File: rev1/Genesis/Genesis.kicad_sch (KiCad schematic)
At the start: 0 parts

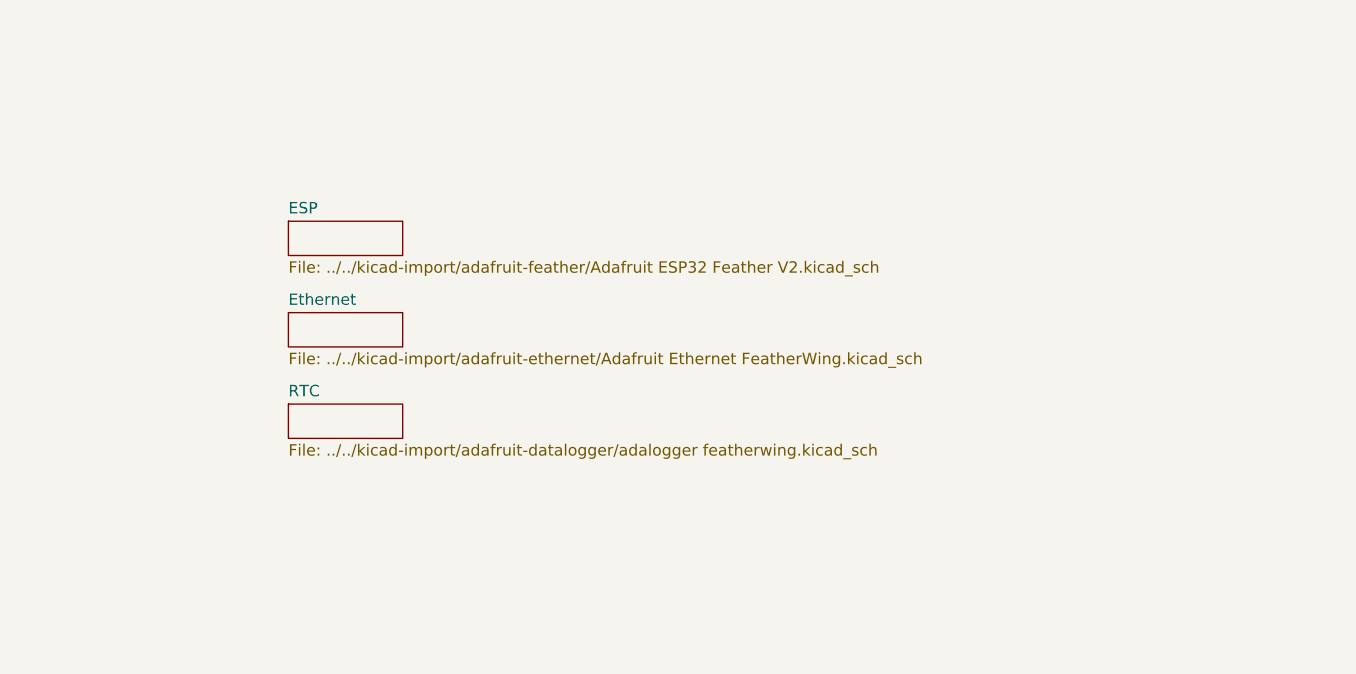
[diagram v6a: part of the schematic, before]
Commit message: Start adding heirarchical labels. Add notes to check sub-feather jumpers.
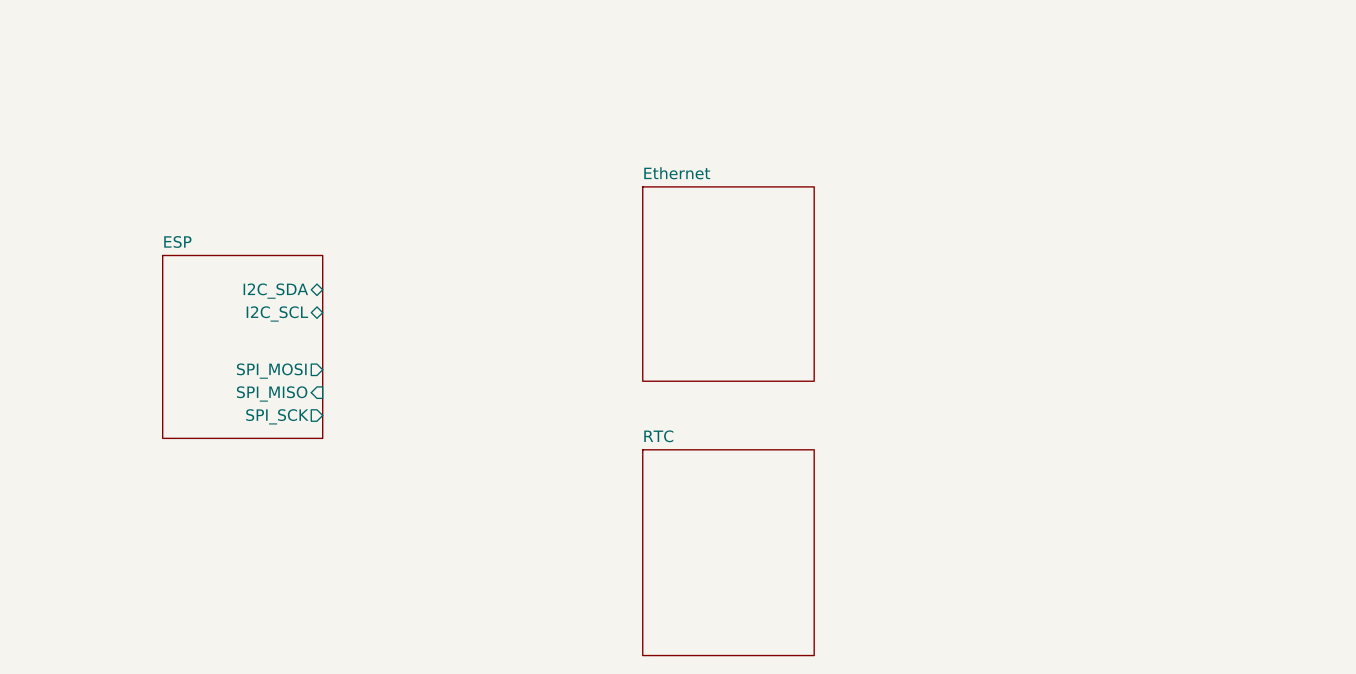
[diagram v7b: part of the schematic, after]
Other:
- sheet ESP ports: added I2C_SCL, I2C_SDA, SPI_MISO, SPI_MOSI, SPI_SCK; removed none
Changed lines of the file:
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@@
 	)
 	(sheet
-		(at 66.04 62.23)
-		(size 12.7 3.81)
+		(at 52.07 66.04)
+		(size 17.78 20.32)
 		(exclude_from_sim no)
 		(in_bom yes)
@@
 		)
 		(property "Sheetname" "ESP"
-			(at 66.04 61.5184 0)
+			(at 52.07 65.3284 0)
 			(effects
 				(font
@@
 		)
 		(property "Sheetfile" "../../kicad-import/adafruit-feather/Adafruit ESP32 Feather V2.kicad_sch"
-			(at 66.04 66.6246 0)
+			(at 52.07 86.9446 0)
 			(effects
 				(font
@@
 				)
 				(justify left top)
+				(hide yes)
+			)
+		)
+		(pin "I2C_SDA" bidirectional
+			(at 69.85 69.85 0)
+			(effects
+				(font
+					(size 1.27 1.27)
+				)
+				(justify right)
+			)
+		)
+		(pin "SPI_MOSI" output
+			(at 69.85 78.74 0)
+			(effects
+				(font
+					(size 1.27 1.27)
+				)
+				(justify right)
+			)
+		)
+		(pin "I2C_SCL" bidirectional
+			(at 69.85 72.39 0)
+			(effects
+				(font
+					(size 1.27 1.27)
+				)
+				(justify right)
+			)
+		)
+		(pin "SPI_MISO" input
+			(at 69.85 81.28 0)
+			(effects
+				(font
+					(size 1.27 1.27)
+				)
+				(justify right)
+			)
+		)
+		(pin "SPI_SCK" output
+			(at 69.85 83.82 0)
+			(effects
+				(font
+					(size 1.27 1.27)
+				)
+				(justify right)
 			)
 		)
@@
 	)
 	(sheet
-		(at 66.04 72.39)
-		(size 12.7 3.81)
+		(at 105.41 58.42)
+		(size 19.05 21.59)
 		(exclude_from_sim no)
 		(in_bom yes)
@@
 		)
 		(property "Sheetname" "Ethernet"
-			(at 66.04 71.6784 0)
+			(at 105.41 57.7084 0)
 			(effects
 				(font
@@
 		)
 		(property "Sheetfile" "../../kicad-import/adafruit-ethernet/Adafruit Ethernet FeatherWing.kicad_sch"
-			(at 66.04 76.7846 0)
+			(at 105.41 80.5946 0)
 			(effects
 				(font
@@
 				)
 				(justify left top)
+				(hide yes)
 			)
 		)
@@
 	)
 	(sheet
-		(at 66.04 82.55)
-		(size 12.7 3.81)
+		(at 105.41 87.63)
+		(size 19.05 22.86)
 		(exclude_from_sim no)
 		(in_bom yes)
@@
 		)
 		(property "Sheetname" "RTC"
-			(at 66.04 81.8384 0)
+			(at 105.41 86.9184 0)
 			(effects
 				(font
@@
 		)
 		(property "Sheetfile" "../../kicad-import/adafruit-datalogger/adalogger featherwing.kicad_sch"
-			(at 66.04 86.9446 0)
+			(at 105.41 111.0746 0)
 			(effects
 				(font
@@
 				)
 				(justify left top)
+				(hide yes)
 			)
 		)

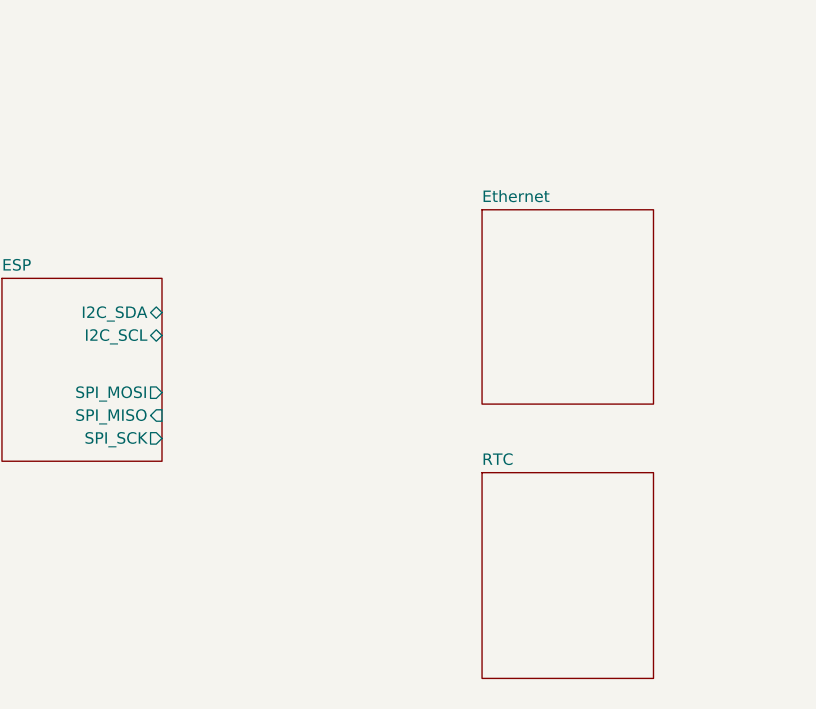
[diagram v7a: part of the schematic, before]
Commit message: Add cross-sheet nets for I2C.
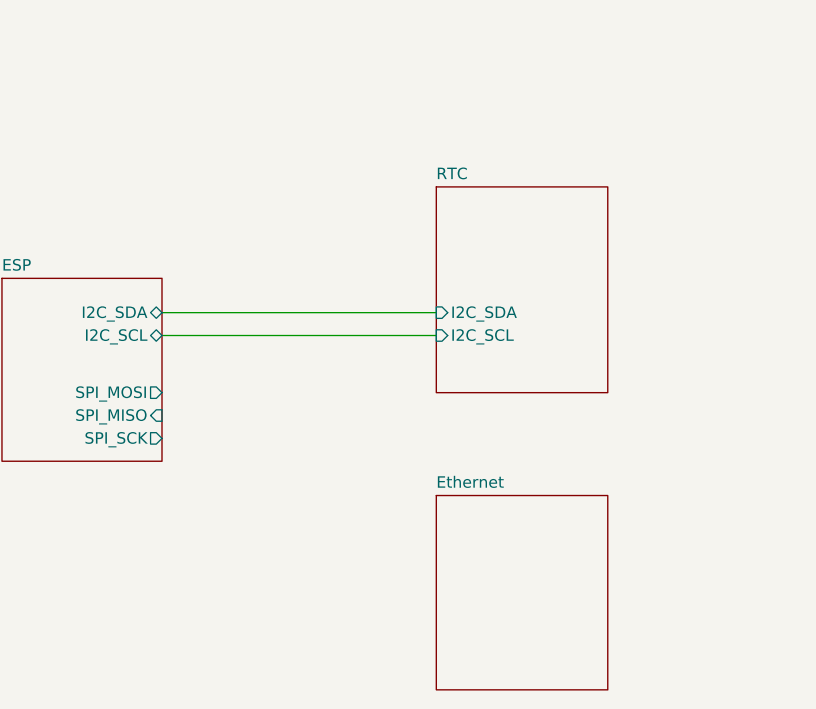
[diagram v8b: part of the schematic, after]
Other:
- sheet RTC ports: added I2C_SCL, I2C_SDA; removed none
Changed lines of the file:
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@@
+		)
+	)
+	(wire
+		(pts
+			(xy 69.85 69.85) (xy 100.33 69.85)
+		)
+		(stroke
+			(width 0)
+			(type default)
+		)
+	)
+	(wire
+		(pts
+			(xy 69.85 72.39) (xy 100.33 72.39)
+		)
+		(stroke
+			(width 0)
+			(type default)
 		)
 	)
@@
 	)
 	(sheet
-		(at 105.41 58.42)
+		(at 100.33 90.17)
 		(size 19.05 21.59)
 		(exclude_from_sim no)
@@
 		)
 		(property "Sheetname" "Ethernet"
-			(at 105.41 57.7084 0)
+			(at 100.33 89.4584 0)
 			(effects
 				(font
@@
 		)
 		(property "Sheetfile" "../../kicad-import/adafruit-ethernet/Adafruit Ethernet FeatherWing.kicad_sch"
-			(at 105.41 80.5946 0)
+			(at 100.33 112.3446 0)
 			(effects
 				(font
@@
 	)
 	(sheet
-		(at 105.41 87.63)
+		(at 100.33 55.88)
 		(size 19.05 22.86)
 		(exclude_from_sim no)
@@
 		)
 		(property "Sheetname" "RTC"
-			(at 105.41 86.9184 0)
+			(at 100.33 55.1684 0)
 			(effects
 				(font
@@
 		)
 		(property "Sheetfile" "../../kicad-import/adafruit-datalogger/adalogger featherwing.kicad_sch"
-			(at 105.41 111.0746 0)
+			(at 100.33 79.3246 0)
 			(effects
 				(font
@@
 			)
 		)
+		(pin "I2C_SDA" input
+			(at 100.33 69.85 180)
+			(effects
+				(font
+					(size 1.27 1.27)
+				)
+				(justify left)
+			)
+		)
+		(pin "I2C_SCL" input
+			(at 100.33 72.39 180)
+			(effects
+				(font
+					(size 1.27 1.27)
+				)
+				(justify left)
+			)
+		)
